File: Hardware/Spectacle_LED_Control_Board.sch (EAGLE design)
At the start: 43 parts, among them J1 FTDI_DEVICE, J3 USB-MICROB, J4 AUDIO-JACK3, J8 AUDIO-JACK3, U1 CY8C4146LQI-S422, U2 3.3V/150mA

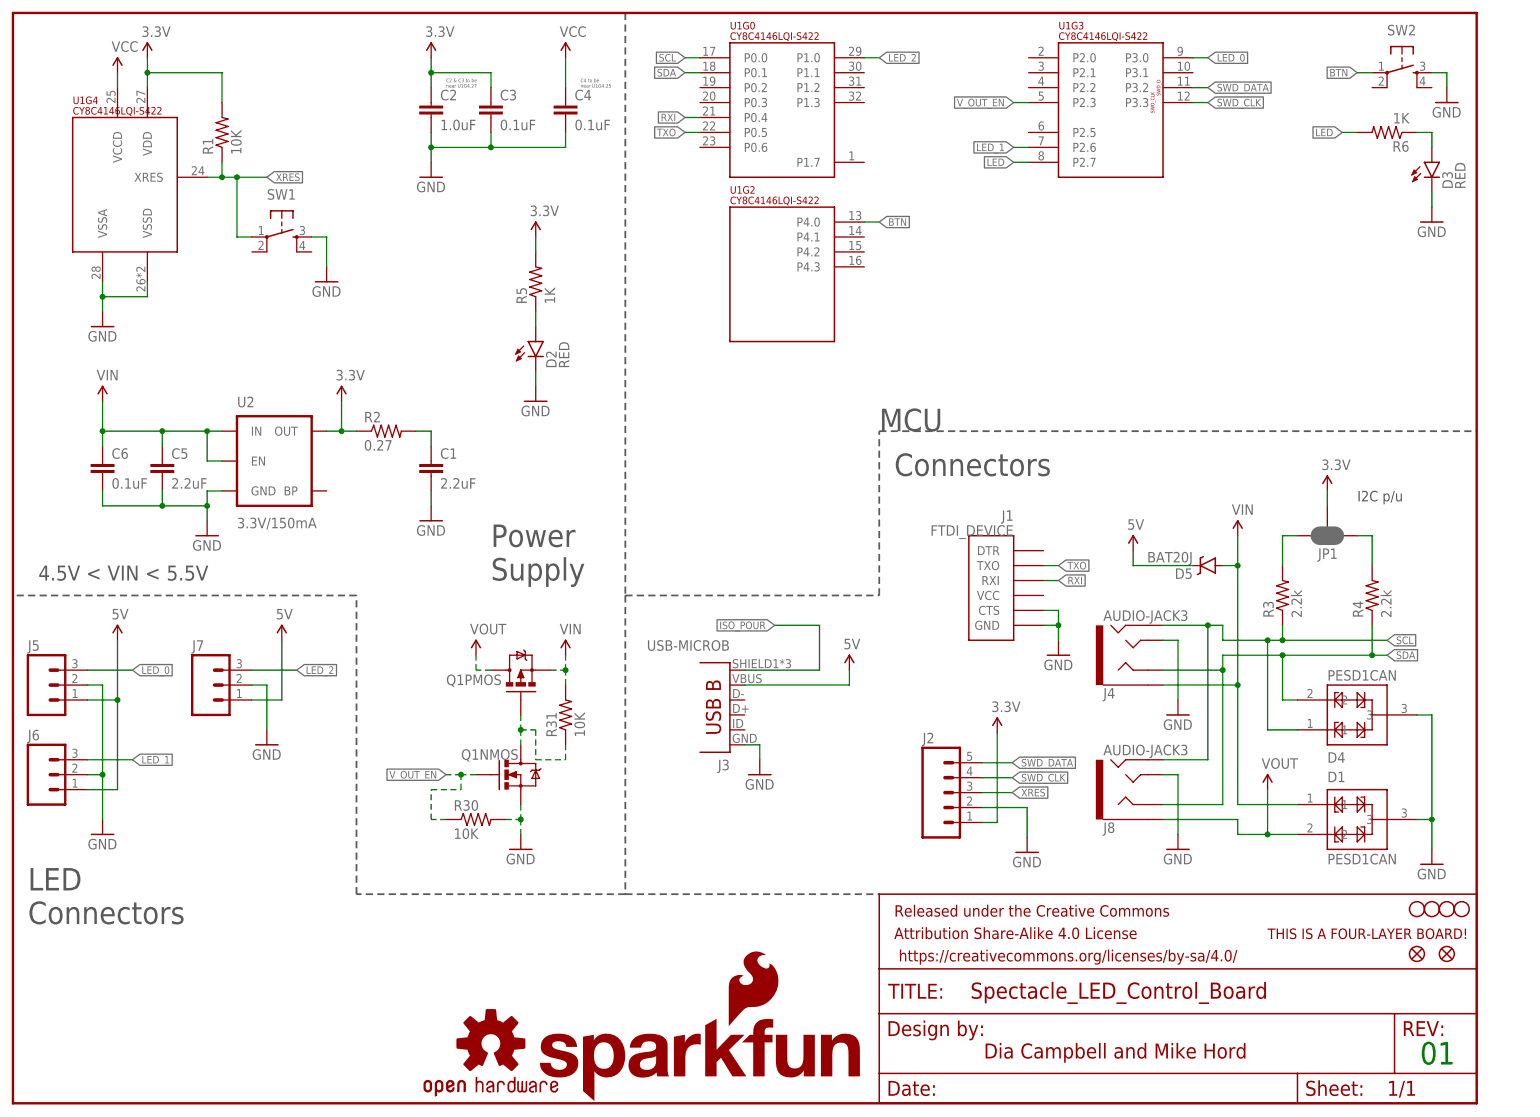
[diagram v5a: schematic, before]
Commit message: Added I2C switching hardware
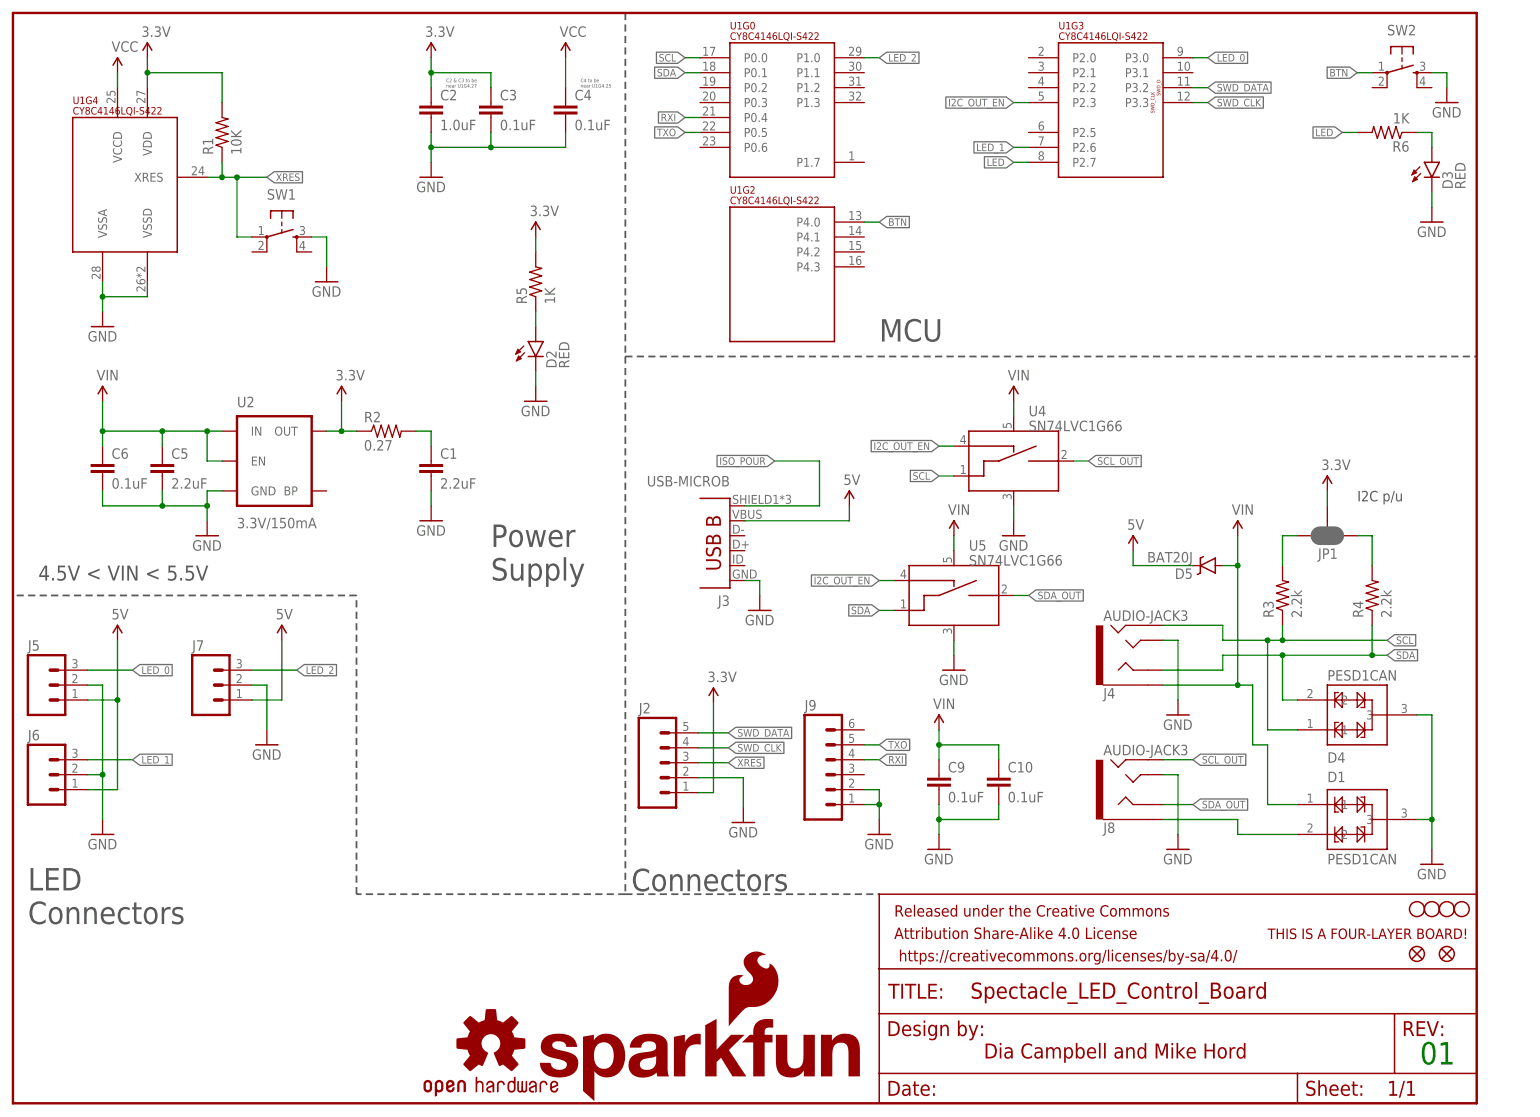
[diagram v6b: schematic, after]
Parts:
- removed J1: FTDI_DEVICE, SparkFun-Connectors:FTDI_DEVICE
- removed Q1: (no value), SparkFun-DiscreteSemi:IRF7509
- removed R30, R31: 10K, SparkFun-Resistors:10KOHM-1/10W-1%(0603)0603
- added C10, C9: 0.1uF, SparkFun-Capacitors:0.1UF-16V(+-10%)(0402)
- added J9: (no value), SparkFun-Connectors:M06NO_SILK_FEMALE_PTH
- added U4, U5: SN74LVC1G66, SparkFun-AnalogIC:SN74LVC1G66_SPST_AMUX
- J2: device SparkFun-Connectors:M05PTH -> SparkFun-Connectors:M05NO_SILK
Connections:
- removed net N$26: Q1NMOS.D, Q1PMOS.G, R31.1
- removed net VOUT: D1.2, J8.EARTH, Q1PMOS.D
- removed net V_OUT_EN: Q1NMOS.G, R30.1, U1G3.P2.3
- new net I2C_OUT_EN: U1G3.P2.3, U4.CTRL_IN, U5.CTRL_IN
- new net N$1: D1.2, J8.EARTH
- new net SCL_OUT: J8.RING2, U4.A_OUT
- new net SDA_OUT: J8.RING1, U5.A_OUT
- net GND: now also C10.2, C9.2, J9.1, J9.2, U4.VSS, U5.VSS; no longer J1.CTS, J1.GND, Q1NMOS.S, R30.2
- net RXI: now also J9.4; no longer J1.RXI
- net SCL: now also U4.A_IN; no longer J8.RING2
- net SDA: now also U5.A_IN; no longer J8.RING1
- net TXO: now also J9.5; no longer J1.TXO
- net VIN: now also C10.1, C9.1, U4.VCC, U5.VCC; no longer Q1PMOS.S, R31.2
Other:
- moved on the sheet: J2, J3

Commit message: File changes from checklist first pass
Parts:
- J5, J6, J7: PROD_ID (none) -> CONN-13230
- J9: device SparkFun-Connectors:M06NO_SILK_FEMALE_PTH -> SparkFun-Connectors:M06NO_SILK_NO_POP
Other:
- note added: "02"
- note removed: "01"
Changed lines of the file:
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@@
 <?xml version="1.0" encoding="utf-8"?>
 <!DOCTYPE eagle SYSTEM "eagle.dtd">
-<eagle version="7.3.0">
+<eagle version="7.7.0">
 <drawing>
 <settings>
@@
 <part name="SUPPLY12" library="SparkFun-Aesthetics" deviceset="5V" device=""/>
 <part name="GND2" library="SparkFun-Aesthetics" deviceset="GND" device=""/>
-<part name="J5" library="SparkFun-Connectors" deviceset="M03" device="JST-PTH-VERT"/>
-<part name="J6" library="SparkFun-Connectors" deviceset="M03" device="JST-PTH-VERT"/>
-<part name="J7" library="SparkFun-Connectors" deviceset="M03" device="JST-PTH-VERT"/>
+<part name="J5" library="SparkFun-Connectors" deviceset="M03" device="JST-PTH-VERT">
+<attribute name="PROD_ID" value="CONN-13230"/>
+</part>
+<part name="J6" library="SparkFun-Connectors" deviceset="M03" device="JST-PTH-VERT">
+<attribute name="PROD_ID" value="CONN-13230"/>
+</part>
+<part name="J7" library="SparkFun-Connectors" deviceset="M03" device="JST-PTH-VERT">
+<attribute name="PROD_ID" value="CONN-13230"/>
+</part>
 <part name="SUPPLY13" library="SparkFun-Aesthetics" deviceset="5V" device=""/>
 <part name="SUPPLY14" library="SparkFun-Aesthetics" deviceset="5V" device=""/>
@@
 <part name="D5" library="SparkFun-DiscreteSemi" deviceset="DIODE-SCHOTTKY" device="-BAT20J" value="BAT20J"/>
 <part name="SUPPLY10" library="SparkFun-Aesthetics" deviceset="5V" device=""/>
-<part name="J9" library="SparkFun-Connectors" deviceset="M06" device="NO_SILK_FEMALE_PTH"/>
+<part name="J9" library="SparkFun-Connectors" deviceset="M06" device="NO_SILK_NO_POP"/>
 <part name="C9" library="SparkFun-Capacitors" deviceset="0.1UF-16V(+-10%)(0402)" device="" value="0.1uF"/>
 <part name="C10" library="SparkFun-Capacitors" deviceset="0.1UF-16V(+-10%)(0402)" device="" value="0.1uF"/>
@@
 <wire x1="58.42" y1="86.36" x2="0" y2="86.36" width="0.3048" layer="97" style="longdash"/>
 <text x="165.1" y="7.62" size="2.54" layer="94" font="vector">Dia Campbell and Mike Hord</text>
-<text x="239.268" y="6.604" size="3.81" layer="91" font="vector">01</text>
+<text x="239.268" y="6.604" size="3.81" layer="91" font="vector">02</text>
 <wire x1="104.14" y1="127" x2="248.92" y2="127" width="0.3048" layer="97" style="longdash"/>
 <text x="147.32" y="129.54" size="3.81" layer="97" font="vector">MCU</text>
@@
 <instance part="SUPPLY12" gate="G$1" x="142.24" y="101.6"/>
 <instance part="GND2" gate="1" x="127" y="83.82"/>
-<instance part="J5" gate="J$1" x="5.08" y="71.12"/>
-<instance part="J6" gate="J$1" x="5.08" y="55.88"/>
-<instance part="J7" gate="J$1" x="33.02" y="71.12"/>
+<instance part="J5" gate="J$1" x="5.08" y="71.12">
+<attribute name="PROD_ID" x="5.08" y="71.12" size="1.778" layer="96" display="off"/>
+</instance>
+<instance part="J6" gate="J$1" x="5.08" y="55.88">
+<attribute name="PROD_ID" x="5.08" y="55.88" size="1.778" layer="96" display="off"/>
+</instance>
+<instance part="J7" gate="J$1" x="33.02" y="71.12">
+<attribute name="PROD_ID" x="33.02" y="71.12" size="1.778" layer="96" display="off"/>
+</instance>
 <instance part="SUPPLY13" gate="G$1" x="17.78" y="78.74"/>
 <instance part="SUPPLY14" gate="G$1" x="45.72" y="78.74"/>
